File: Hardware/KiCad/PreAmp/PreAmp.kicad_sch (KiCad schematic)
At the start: 17 parts, among them J1 Conn_01x05_Pin, J2 Conn_01x03_Pin, J3 XLR3, U1 TLV2371DBV, U2 INA217AIDWR

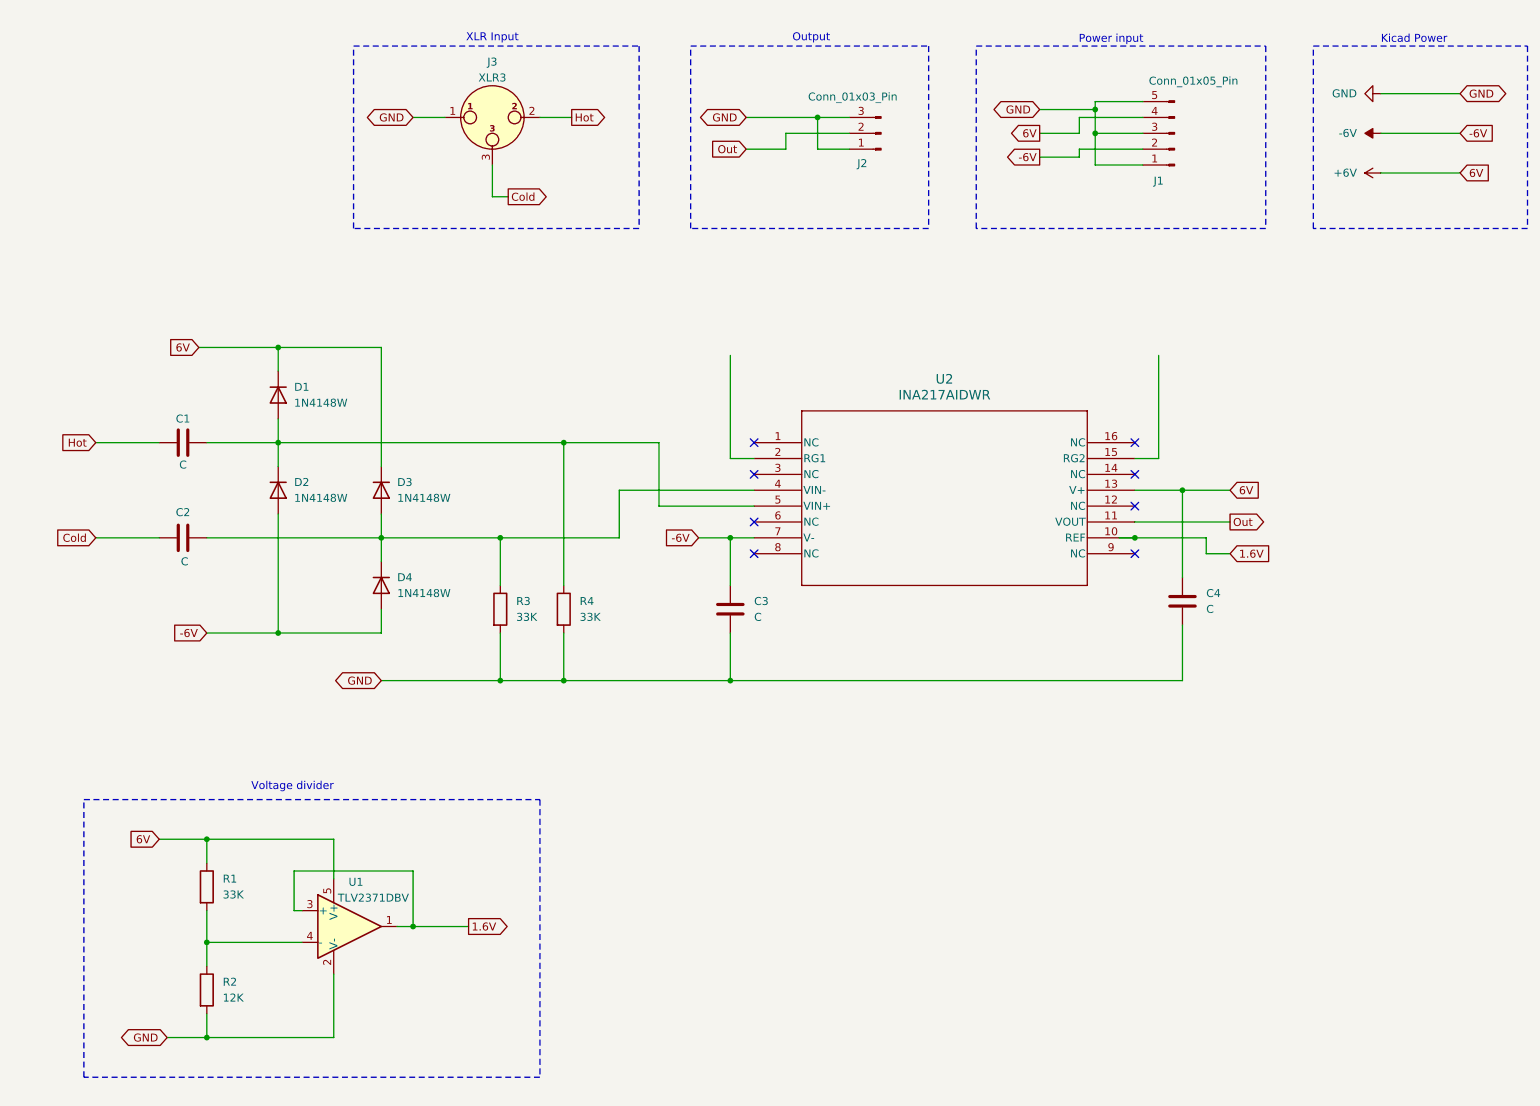
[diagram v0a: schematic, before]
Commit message: Potmeter for amplification
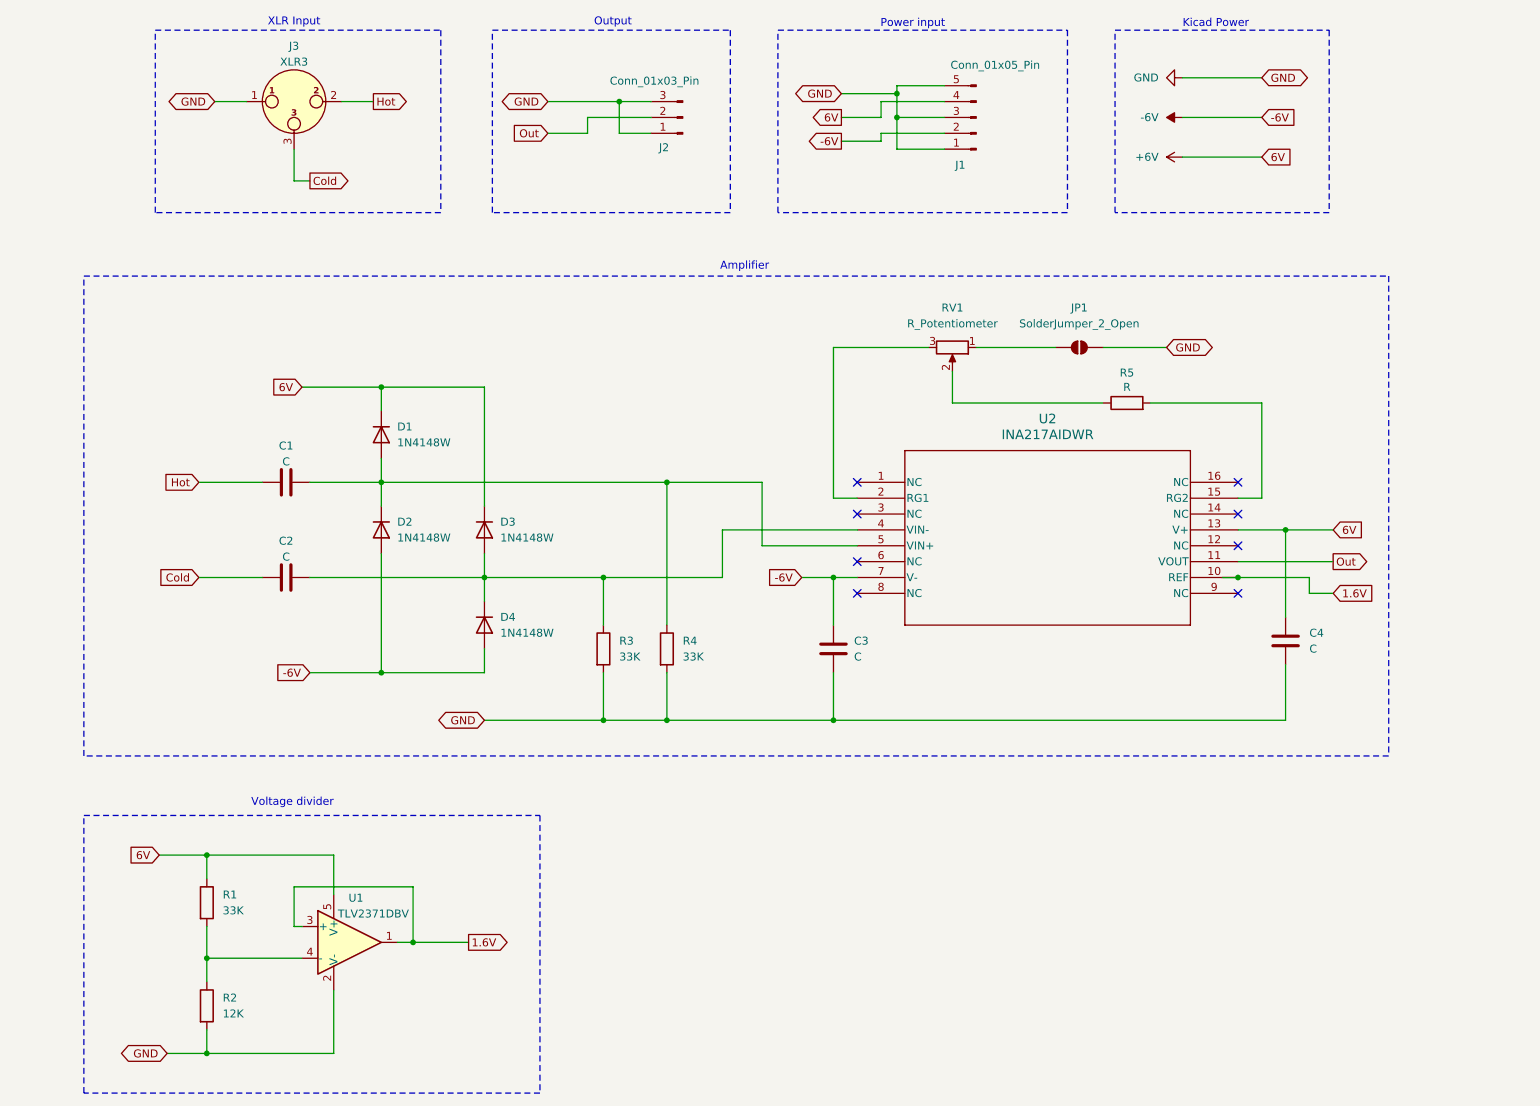
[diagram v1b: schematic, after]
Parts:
- added JP1: SolderJumper_2_Open, symbol Jumper:SolderJumper_2_Open
- added R5: R, symbol Device:R
- added RV1: R_Potentiometer, Potentiometer_THT:Potentiometer_Alpha_RD901F-40-00D_Single_Vertical, symbol Device:R_Potentiometer
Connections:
- net GND: now also JP1.2 (B)
- net at U2.15 (RG2): now also R5.2
- net at U2.2 (RG1): now also RV1.3
- new net: JP1.1 (A), RV1.1
- new net: R5.1, RV1.2
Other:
- note added: "Amplifier"
- moved on the sheet: C3, C4, D1, D2, D3, D4, J1, J2, J3, R1, R2, R3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

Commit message: Datasheet comments + extra test points added
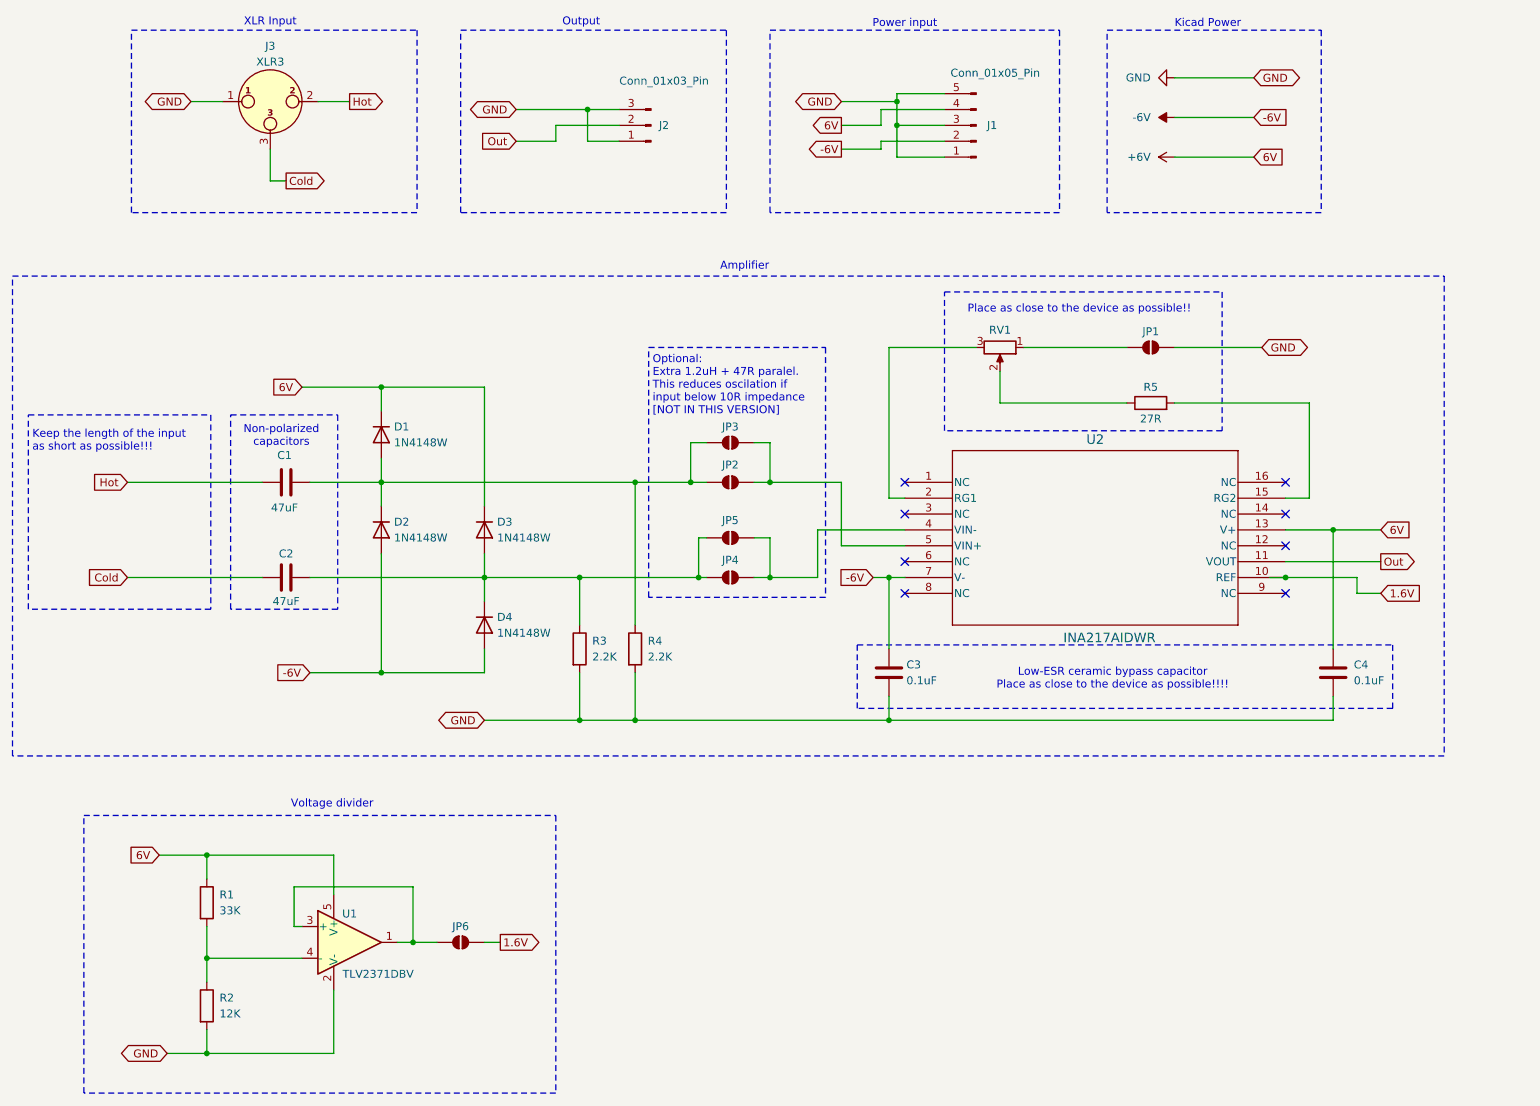
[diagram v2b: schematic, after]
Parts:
- added JP2, JP3, JP4, JP5, JP6: SolderJumper_2_Open, symbol Jumper:SolderJumper_2_Open
- C1, C2: value C -> 47uF
- C3, C4: value C -> 0.1uF
- R3, R4: value 33K -> 2.2K
- R5: value R -> 27R
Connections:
- net 1.6V: now also JP6.2 (B); no longer U1.1, U1.3 (+)
- net at C1.2, D1.2 (A), D2.1 (K)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: now also JP2.1 (A), JP3.1 (A); no longer U2.5 (VIN+)
- net at C2.2, D3.2 (A), D4.1 (K)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: now also JP4.1 (A), JP5.1 (A); no longer U2.4 (VIN-)
- new net: JP4.2 (B), JP5.2 (B), U2.4 (VIN-)
- new net: JP2.2 (B), JP3.2 (B), U2.5 (VIN+)
- new net: JP6.1 (A), U1.1, U1.3 (+)
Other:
- note added: "Keep the length of the input as short as possible!!!"
- note added: "Low-ESR ceramic bypass capacitor Place as close to the device as possible!!!!"
- note added: "Non-polarized capacitors"
- note added: "Optional: Extra 1.2uH + 47R paralel. This reduces oscilation if input below 10R impedance [NOT IN THIS VERSION]"
- note added: "Place as close to the device as possible!!"
- moved on the sheet: C3, C4, J1, J2, J3, JP1, R3, R4, R5, RV1, U2
